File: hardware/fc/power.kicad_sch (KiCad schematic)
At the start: 26 parts, among them U1 TPS7A8101DRBR, U2 TPS7A8101DRBR, U3 LMR51420YFDDCR

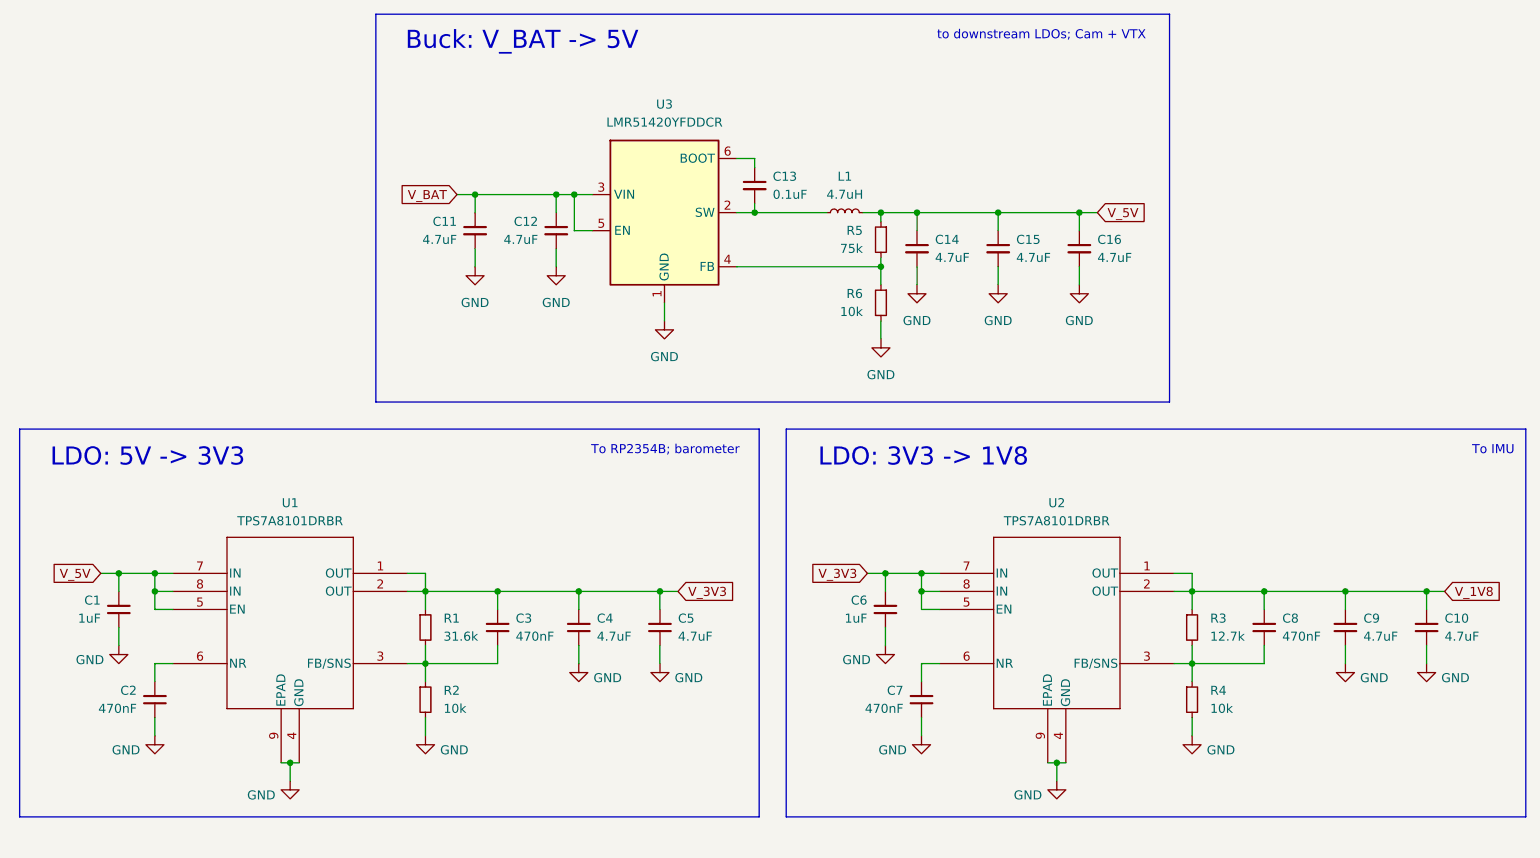
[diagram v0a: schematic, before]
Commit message: fc: add peripherals and sensors
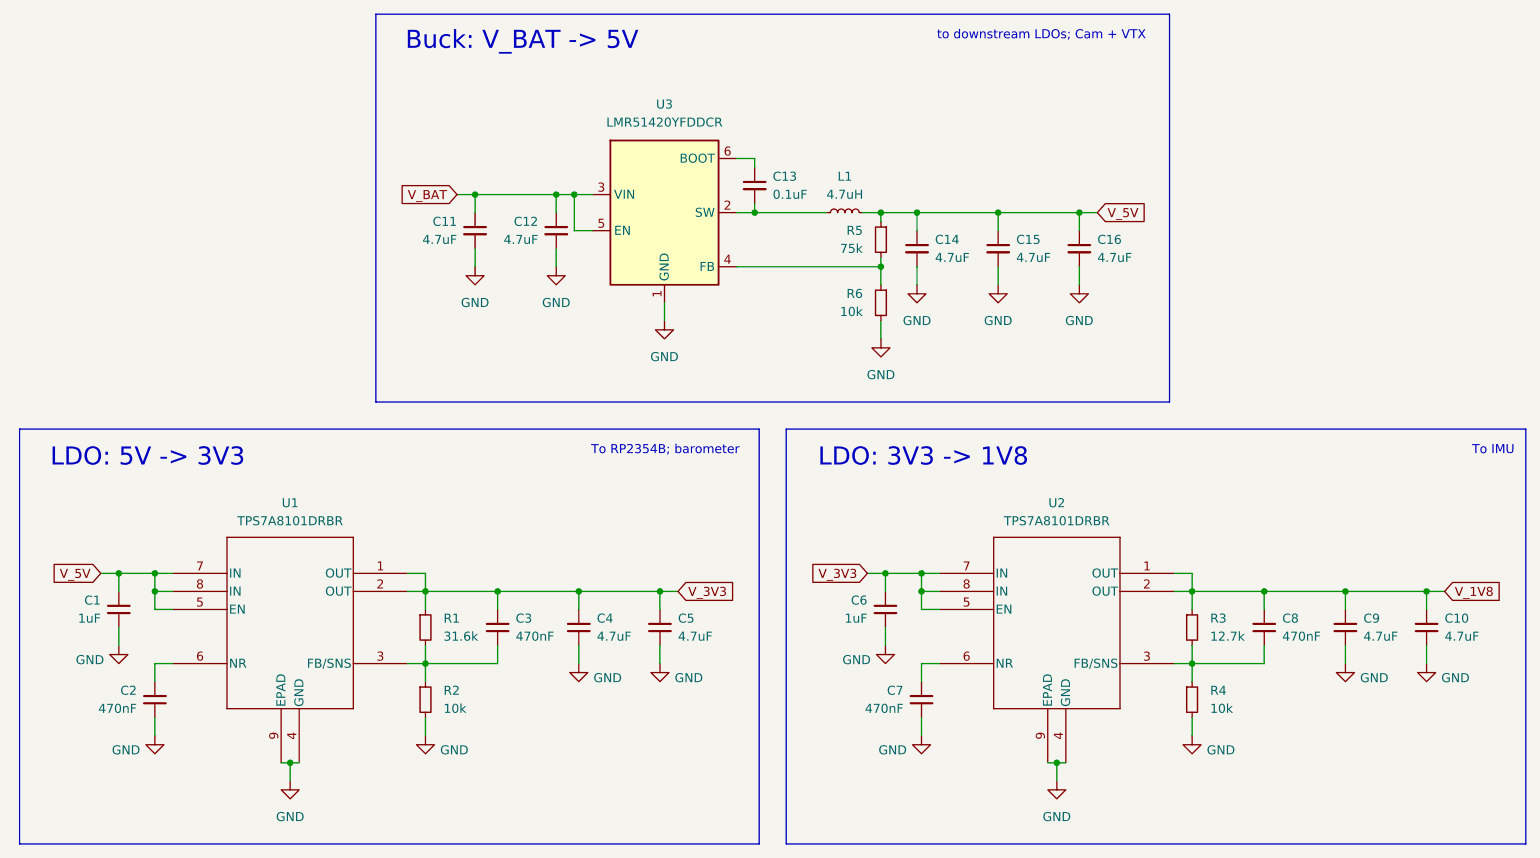
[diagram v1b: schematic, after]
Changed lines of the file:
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@@
 	(rectangle
 		(start 149.86 92.71)
-		(end 254 147.32)
+		(end 254 151.13)
 		(stroke
 			(width 0)
@@
 	(rectangle
 		(start 41.91 92.71)
-		(end 146.05 147.32)
+		(end 146.05 151.13)
 		(stroke
 			(width 0)
@@
 	(symbol
 		(lib_id "power:GND")
-		(at 187.96 142.24 0)
-		(unit 1)
-		(body_style 1)
-		(exclude_from_sim no)
-		(in_bom yes)
-		(on_board yes)
-		(in_pos_files yes)
-		(dnp no)
-		(property "Reference" "#PWR08"
-			(at 187.96 148.59 0)
-			(hide yes)
-			(show_name no)
-			(do_not_autoplace no)
-			(effects
-				(font
-					(size 1.27 1.27)
-				)
-			)
-		)
-		(property "Value" "GND"
-			(at 183.896 144.272 0)
-			(show_name no)
-			(do_not_autoplace no)
-			(effects
-				(font
-					(size 1.27 1.27)
-				)
-			)
-		)
-		(property "Footprint" ""
-			(at 187.96 142.24 0)
-			(hide yes)
-			(show_name no)
-			(do_not_autoplace no)
-			(effects
-				(font
-					(size 1.27 1.27)
-				)
-			)
-		)
-		(property "Datasheet" ""
-			(at 187.96 142.24 0)
-			(hide yes)
-			(show_name no)
-			(do_not_autoplace no)
-			(effects
-				(font
-					(size 1.27 1.27)
-				)
-			)
-		)
-		(property "Description" "Power symbol creates a global label with name \"GND\" , ground"
-			(at 187.96 142.24 0)
-			(hide yes)
-			(show_name no)
-			(do_not_autoplace no)
-			(effects
-				(font
-					(size 1.27 1.27)
-				)
-			)
-		)
-		(pin "1"
-		)
-		(instances
-			(project "fc"
-				(path "/6eb6d89e-9d71-4347-9ba3-a394c00e5720/e2294782-fc96-4933-bb6d-aced2c760448"
-					(reference "#PWR08")
-					(unit 1)
-				)
-			)
-		)
-	)
-	(symbol
-		(lib_id "power:GND")
 		(at 120.65 125.73 0)
 		(mirror y)
@@
 	(symbol
 		(lib_id "power:GND")
-		(at 132.715 77.47 0)
+		(at 187.96 142.24 0)
 		(unit 1)
 		(body_style 1)
@@
 		(dnp no)
 		(fields_autoplaced yes)
-		(property "Reference" "#PWR065"
-			(at 132.715 83.82 0)
+		(property "Reference" "#PWR08"
+			(at 187.96 148.59 0)
 			(hide yes)
 			(show_name no)
@@
 		)
 		(property "Value" "GND"
-			(at 132.715 82.55 0)
+			(at 187.96 147.32 0)
 			(show_name no)
 			(do_not_autoplace no)
@@
 		)
 		(property "Footprint" ""
-			(at 132.715 77.47 0)
+			(at 187.96 142.24 0)
 			(hide yes)
 			(show_name no)
@@
 		)
 		(property "Datasheet" ""
-			(at 132.715 77.47 0)
+			(at 187.96 142.24 0)
 			(hide yes)
 			(show_name no)
@@
 		)
 		(property "Description" "Power symbol creates a global label with name \"GND\" , ground"
-			(at 132.715 77.47 0)
+			(at 187.96 142.24 0)
 			(hide yes)
 			(show_name no)
@@
 			(project "fc"
 				(path "/6eb6d89e-9d71-4347-9ba3-a394c00e5720/e2294782-fc96-4933-bb6d-aced2c760448"
-					(reference "#PWR065")
+					(reference "#PWR08")
 					(unit 1)
 				)
@@
 	)
 	(symbol
-		(lib_name "C_Small_6")
-		(lib_id "Device:C_Small")
-		(at 117.475 64.77 0)
-		(mirror y)
+		(lib_id "power:GND")
+		(at 132.715 77.47 0)
 		(unit 1)
 		(body_style 1)
@@
 		(in_pos_files yes)
 		(dnp no)
-		(property "Reference" "C12"
-			(at 114.935 63.5062 0)
+		(fields_autoplaced yes)
+		(property "Reference" "#PWR065"
+			(at 132.715 83.82 0)
+			(hide yes)
 			(show_name no)
 			(do_not_autoplace no)
@@
 					(size 1.27 1.27)
 				)
-				(justify left)
 			)
 		)
-		(property "Value" "4.7uF"
-			(at 114.935 66.0462 0)
+		(property "Value" "GND"
+			(at 132.715 82.55 0)
 			(show_name no)
 			(do_not_autoplace no)
@@
 					(size 1.27 1.27)
 				)
-				(justify left)
 			)
 		)
-		(property "Footprint" "Capacitor_SMD:C_0603_1608Metric"
-			(at 117.475 64.77 0)
+		(property "Footprint" ""
+			(at 132.715 77.47 0)
 			(hide yes)
 			(show_name no)
@@
 		)
 		(property "Datasheet" ""
-			(at 117.475 64.77 0)
+			(at 132.715 77.47 0)
 			(hide yes)
 			(show_name no)
@@
 			)
 		)
-		(property "Description" "0603 4.7uF 35V"
-			(at 117.475 64.77 0)
+		(property "Description" "Power symbol creates a global label with name \"GND\" , ground"
+			(at 132.715 77.47 0)
 			(hide yes)
 			(show_name no)
@@
 			)
 		)
-		(property "LCSC#" "C307467"
-			(at 117.475 64.77 0)
+		(pin "1"
+		)
+		(instances
+			(project "fc"
+				(path "/6eb6d89e-9d71-4347-9ba3-a394c00e5720/e2294782-fc96-4933-bb6d-aced2c760448"
+					(reference "#PWR065")
+					(unit 1)
+				)
+			)
+		)
+	)
+	(symbol
+		(lib_id "power:GND")
+		(at 80.01 142.24 0)
+		(unit 1)
+		(body_style 1)
+		(exclude_from_sim no)
+		(in_bom yes)
+		(on_board yes)
+		(in_pos_files yes)
+		(dnp no)
+		(fields_autoplaced yes)
+		(property "Reference" "#PWR03"
+			(at 80.01 148.59 0)
 			(hide yes)
 			(show_name no)
@@
 			)
 		)
-		(property "MFR" "Samsung"
-			(at 117.475 64.77 0)
+		(property "Value" "GND"
+			(at 80.01 147.32 0)
+			(show_name no)
+			(do_not_autoplace no)
+			(effects
+				(font
+					(size 1.27 1.27)
+				)
+			)
+		)
+		(property "Footprint" ""
+			(at 80.01 142.24 0)
 			(hide yes)
 			(show_name no)
@@
 			)
 		)
-		(property "MPN" "CL10A475KL8NRNC"
-			(at 117.475 64.77 0)
+		(property "Datasheet" ""
+			(at 80.01 142.24 0)
 			(hide yes)
 			(show_name no)
@@
 			)
 		)
-		(pin "1"
+		(property "Description" "Power symbol creates a global label with name \"GND\" , ground"
+			(at 80.01 142.24 0)
+			(hide yes)
+			(show_name no)
+			(do_not_autoplace no)
+			(effects
+				(font
+					(size 1.27 1.27)
+				)
+			)
 		)
-		(pin "2"
+		(pin "1"
 		)
 		(instances
 			(project "fc"
 				(path "/6eb6d89e-9d71-4347-9ba3-a394c00e5720/e2294782-fc96-4933-bb6d-aced2c760448"
-					(reference "C12")
+					(reference "#PWR03")
 					(unit 1)
 				)
@@
 	)
 	(symbol
-		(lib_id "Device:R_Small")
-		(at 99.06 120.65 0)
+		(lib_name "C_Small_6")
+		(lib_id "Device:C_Small")
+		(at 117.475 64.77 0)
+		(mirror y)
 		(unit 1)
 		(body_style 1)
@@
 		(in_pos_files yes)
 		(dnp no)
-		(fields_autoplaced yes)
-		(property "Reference" "R1"
-			(at 101.6 119.3799 0)
+		(property "Reference" "C12"
+			(at 114.935 63.5062 0)
 			(show_name no)
 			(do_not_autoplace no)
@@
 			)
 		)
-		(property "Value" "31.6k"
-			(at 101.6 121.9199 0)
+		(property "Value" "4.7uF"
+			(at 114.935 66.0462 0)
 			(show_name no)
 			(do_not_autoplace no)
@@
 			)
 		)
-		(property "Footprint" ""
-			(at 99.06 120.65 0)
+		(property "Footprint" "Capacitor_SMD:C_0603_1608Metric"
+			(at 117.475 64.77 0)
 			(hide yes)
 			(show_name no)
@@
 		)
 		(property "Datasheet" ""
-			(at 99.06 120.65 0)
+			(at 117.475 64.77 0)
 			(hide yes)
 			(show_name no)
@@
 			)
 		)
-		(property "Description" "Resistor, small symbol"
-			(at 99.06 120.65 0)
+		(property "Description" "0603 4.7uF 35V"
+			(at 117.475 64.77 0)
+			(hide yes)
+			(show_name no)
+			(do_not_autoplace no)
+			(effects
+				(font
+					(size 1.27 1.27)
+				)
+			)
+		)
+		(property "LCSC#" "C307467"
+			(at 117.475 64.77 0)
+			(hide yes)
+			(show_name no)
+			(do_not_autoplace no)
+			(effects
+				(font
+					(size 1.27 1.27)
+				)
+			)
+		)
+		(property "MFR" "Samsung"
+			(at 117.475 64.77 0)
+			(hide yes)
+			(show_name no)
+			(do_not_autoplace no)
+			(effects
+				(font
+					(size 1.27 1.27)
+				)
+			)
+		)
+		(property "MPN" "CL10A475KL8NRNC"
+			(at 117.475 64.77 0)
 			(hide yes)
 			(show_name no)
@@
 			(project "fc"
 				(path "/6eb6d89e-9d71-4347-9ba3-a394c00e5720/e2294782-fc96-4933-bb6d-aced2c760448"
-					(reference "R1")
+					(reference "C12")
 					(unit 1)
 				)
@@
 	)
 	(symbol
-		(lib_id "power:GND")
-		(at 80.01 142.24 0)
+		(lib_id "Device:R_Small")
+		(at 99.06 120.65 0)
 		(unit 1)
 		(body_style 1)
@@
 		(in_pos_files yes)
 		(dnp no)
-		(property "Reference" "#PWR03"
-			(at 80.01 148.59 0)
-			(hide yes)
+		(fields_autoplaced yes)
+		(property "Reference" "R1"
+			(at 101.6 119.3799 0)
 			(show_name no)
 			(do_not_autoplace no)
@@
 					(size 1.27 1.27)
 				)
+				(justify left)
 			)
 		)
-		(property "Value" "GND"
-			(at 75.946 144.272 0)
+		(property "Value" "31.6k"
+			(at 101.6 121.9199 0)
 			(show_name no)
 			(do_not_autoplace no)
@@
 					(size 1.27 1.27)
 				)
+				(justify left)
 			)
 		)
 		(property "Footprint" ""
-			(at 80.01 142.24 0)
+			(at 99.06 120.65 0)
 			(hide yes)
 			(show_name no)
@@
 		)
 		(property "Datasheet" ""
-			(at 80.01 142.24 0)
+			(at 99.06 120.65 0)
 			(hide yes)
 			(show_name no)
@@
 			)
 		)
-		(property "Description" "Power symbol creates a global label with name \"GND\" , ground"
-			(at 80.01 142.24 0)
+		(property "Description" "Resistor, small symbol"
+			(at 99.06 120.65 0)
 			(hide yes)
 			(show_name no)
@@
 		(pin "1"
 		)
+		(pin "2"
+		)
 		(instances
 			(project "fc"
 				(path "/6eb6d89e-9d71-4347-9ba3-a394c00e5720/e2294782-fc96-4933-bb6d-aced2c760448"
-					(reference "#PWR03")
+					(reference "R1")
 					(unit 1)
 				)

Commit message: fc: add 5V mux and OSD
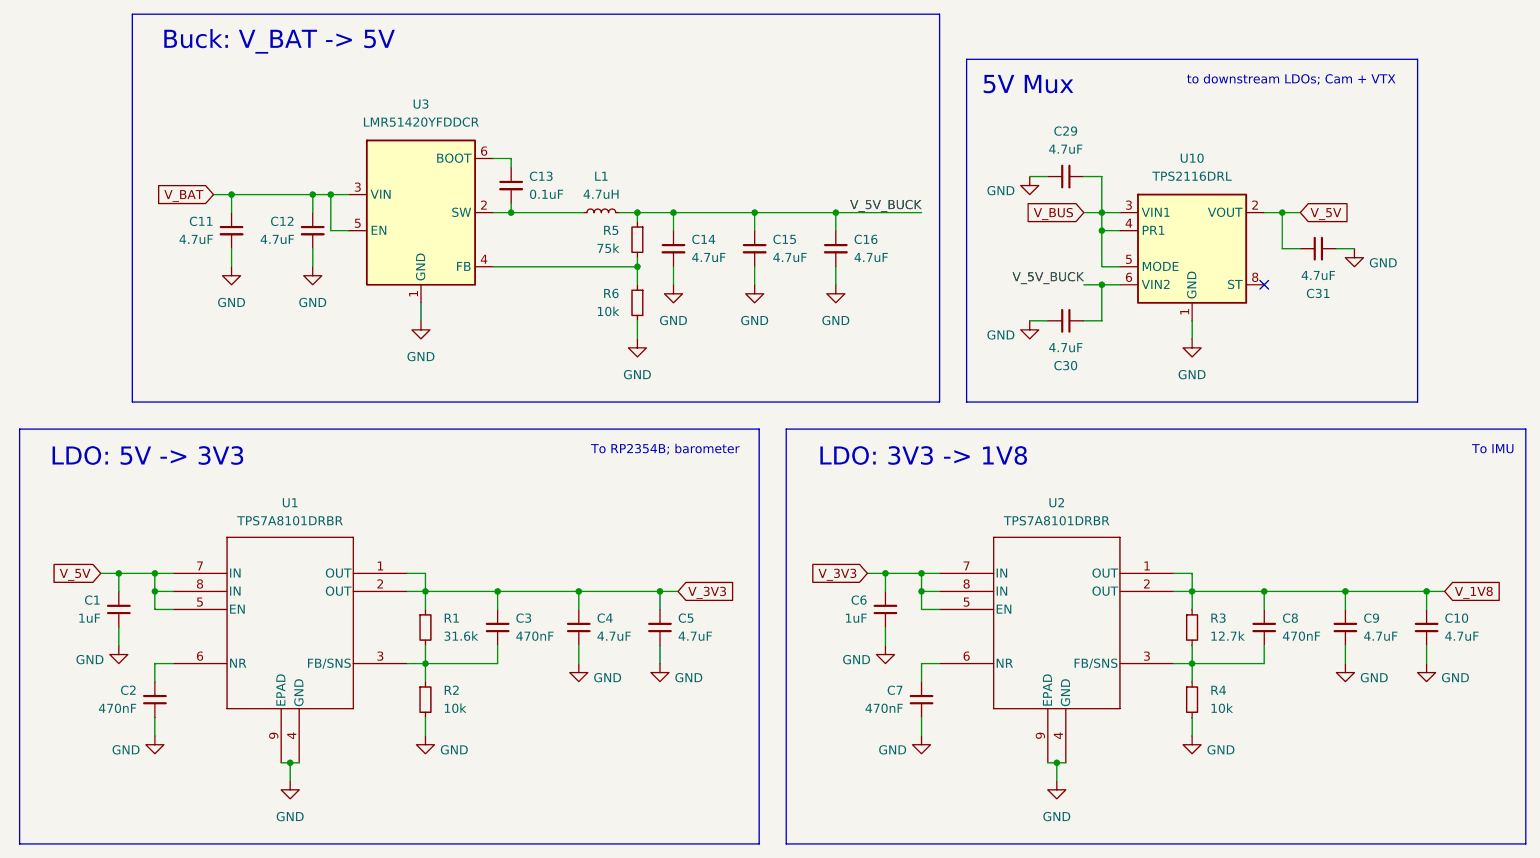
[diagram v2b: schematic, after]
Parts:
- added C29, C30, C31: 4.7uF, Package_TO_SOT_SMD:SOT-583-8, symbol Device:C_Small
- added U10: TPS2116DRL, Package_TO_SOT_SMD:SOT-583-8, symbol Power_Management:TPS2116DRL
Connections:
- net GND: now also C29.2, C30.2, C31.2, U10.1 (GND)
- net V_5V: now also C31.1, U10.2 (VOUT), U10.7 (VOUT); no longer C14.1, C15.1, C16.1, L1.2, R5.1
- new net V_5V_BUCK: C14.1, C15.1, C16.1, C30.1, L1.2, R5.1, U10.6 (VIN2)
- new net V_BUS: C29.1, U10.3 (VIN1), U10.4 (PR1), U10.5 (MODE)
- no-connect marks 0 -> 1
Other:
- note added: "5V Mux"
- moved on the sheet: C11, C12, C13, C14, C15, C16, L1, R5, R6, U3

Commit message: fc: delete barometer; finalise schematic
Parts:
- R3: value 12.7k -> 31.6k
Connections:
- net V_3V3: no longer C6.1, U2.5 (EN), U2.7 (IN), U2.8 (IN)
- net V_5V: now also C6.1, U2.5 (EN), U2.7 (IN), U2.8 (IN)
- net V_1V8 renamed V_IMU
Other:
- note added: "To RP2354B"
- note removed: "LDO: 3V3 -> 1V8"
- note removed: "To RP2354B; barometer"
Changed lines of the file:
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@@
 		)
 	)
-	(text "To RP2354B; barometer"
+	(text "To RP2354B\n"
 		(exclude_from_sim no)
-		(at 132.842 95.758 0)
+		(at 138.43 95.758 0)
 		(effects
 			(font
@@
 		)
 	)
-	(text "LDO: 3V3 -> 1V8"
+	(text "LDO: 5V -> 3V3"
 		(exclude_from_sim no)
-		(at 169.164 96.774 0)
+		(at 167.894 96.774 0)
 		(effects
 			(font
@@
 		)
 	)
-	(global_label "V_3V3"
+	(global_label "V_BUS"
 		(shape input)
-		(at 161.29 113.03 180)
+		(at 191.77 62.23 180)
 		(fields_autoplaced yes)
 		(effects
@@
 		)
 		(property "Intersheetrefs" "${INTERSHEET_REFS}"
-			(at 152.741 113.03 0)
+			(at 182.9186 62.23 0)
 			(hide yes)
 			(show_name no)
@@
 		)
 	)
-	(global_label "V_BUS"
+	(global_label "V_3V3"
 		(shape input)
-		(at 191.77 62.23 180)
+		(at 134.62 115.57 0)
 		(fields_autoplaced yes)
 		(effects
@@
 				(size 1.27 1.27)
 			)
-			(justify right)
+			(justify left)
 		)
 		(property "Intersheetrefs" "${INTERSHEET_REFS}"
-			(at 182.9186 62.23 0)
+			(at 143.169 115.57 0)
 			(hide yes)
 			(show_name no)
@@
 					(size 1.27 1.27)
 				)
-				(justify right)
+				(justify left)
 			)
 		)
 	)
-	(global_label "V_3V3"
+	(global_label "V_5V"
 		(shape input)
-		(at 134.62 115.57 0)
+		(at 53.34 113.03 180)
 		(fields_autoplaced yes)
 		(effects
@@
 				(size 1.27 1.27)
 			)
-			(justify left)
+			(justify right)
 		)
 		(property "Intersheetrefs" "${INTERSHEET_REFS}"
-			(at 143.169 115.57 0)
+			(at 46.0005 113.03 0)
 			(hide yes)
 			(show_name no)
@@
 					(size 1.27 1.27)
 				)
-				(justify left)
+				(justify right)
 			)
 		)
@@
 	(global_label "V_5V"
 		(shape input)
-		(at 53.34 113.03 180)
+		(at 161.29 113.03 180)
 		(fields_autoplaced yes)
 		(effects
@@
 		)
 		(property "Intersheetrefs" "${INTERSHEET_REFS}"
-			(at 46.0005 113.03 0)
+			(at 153.9505 113.03 0)
 			(hide yes)
 			(show_name no)
@@
 		)
 	)
-	(global_label "V_1V8"
+	(global_label "V_IMU"
 		(shape input)
 		(at 242.57 115.57 0)
@@
 		)
 		(property "Intersheetrefs" "${INTERSHEET_REFS}"
-			(at 251.119 115.57 0)
+			(at 250.9981 115.57 0)
 			(hide yes)
 			(show_name no)
@@
 			)
 		)
-		(property "Value" "12.7k"
+		(property "Value" "31.6k"
 			(at 209.55 121.9199 0)
 			(show_name no)

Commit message: fc: add footprints
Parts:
- C1, C10, C2, C3, C4, C5, C6, C7, C8, C9: footprint (none) -> Stratus:C_0402
- C29, C30, C31: footprint Package_TO_SOT_SMD:SOT-583-8 -> Stratus:C_0402
- R1, R2, R3, R4: footprint (none) -> Stratus:R_0402
- U1, U2: footprint Stratus:LDLPUR212 -> Package_SON:VSON-8-1EP_3x3mm_P0.65mm_EP1.65x2.4mm
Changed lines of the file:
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@@
 			)
 		)
-		(property "Footprint" ""
+		(property "Footprint" "Stratus:C_0402"
 			(at 240.03 120.65 0)
 			(hide yes)
@@
 			)
 		)
-		(property "Footprint" ""
+		(property "Footprint" "Stratus:C_0402"
 			(at 60.96 130.81 0)
 			(hide yes)
@@
 			)
 		)
-		(property "Footprint" ""
+		(property "Footprint" "Stratus:C_0402"
 			(at 163.83 118.11 0)
 			(hide yes)
@@
 			)
 		)
-		(property "Footprint" ""
+		(property "Footprint" "Stratus:C_0402"
 			(at 217.17 120.65 0)
 			(hide yes)
@@
 			)
 		)
-		(property "Footprint" ""
+		(property "Footprint" "Stratus:C_0402"
 			(at 120.65 120.65 0)
 			(hide yes)
@@
 			)
 		)
-		(property "Footprint" ""
+		(property "Footprint" "Stratus:R_0402"
 			(at 99.06 130.81 0)
 			(hide yes)
@@
 			)
 		)
-		(property "Footprint" "Package_TO_SOT_SMD:SOT-583-8"
+		(property "Footprint" "Stratus:C_0402"
 			(at 224.79 67.31 0)
 			(hide yes)
@@
 			)
 		)
-		(property "Footprint" ""
+		(property "Footprint" "Stratus:C_0402"
 			(at 109.22 120.65 0)
 			(hide yes)
@@
 			)
 		)
-		(property "Footprint" ""
+		(property "Footprint" "Stratus:R_0402"
 			(at 99.06 120.65 0)
 			(hide yes)
@@
 			)
 		)
-		(property "Footprint" "Stratus:LDLPUR212"
+		(property "Footprint" "Package_SON:VSON-8-1EP_3x3mm_P0.65mm_EP1.65x2.4mm"
 			(at 130.81 114.3 0)
 			(hide yes)
@@
 			)
 		)
-		(property "Footprint" ""
+		(property "Footprint" "Stratus:C_0402"
 			(at 228.6 120.65 0)
 			(hide yes)
@@
 			)
 		)
-		(property "Footprint" ""
+		(property "Footprint" "Stratus:R_0402"
 			(at 207.01 130.81 0)
 			(hide yes)
@@
 			)
 		)
-		(property "Footprint" "Package_TO_SOT_SMD:SOT-583-8"
+		(property "Footprint" "Stratus:C_0402"
 			(at 189.23 57.15 0)
 			(hide yes)
@@
 			)
 		)
-		(property "Footprint" ""
+		(property "Footprint" "Stratus:C_0402"
 			(at 55.88 118.11 0)
 			(hide yes)
@@
 			)
 		)
-		(property "Footprint" ""
+		(property "Footprint" "Stratus:C_0402"
 			(at 132.08 120.65 0)
 			(hide yes)
@@
 			)
 		)
-		(property "Footprint" "Package_TO_SOT_SMD:SOT-583-8"
+		(property "Footprint" "Stratus:C_0402"
 			(at 189.23 77.47 0)
 			(hide yes)
@@
 			)
 		)
-		(property "Footprint" ""
+		(property "Footprint" "Stratus:C_0402"
 			(at 168.91 130.81 0)
 			(hide yes)
@@
 			)
 		)
-		(property "Footprint" ""
+		(property "Footprint" "Stratus:R_0402"
 			(at 207.01 120.65 0)
 			(hide yes)
@@
 			)
 		)
-		(property "Footprint" "Stratus:LDLPUR212"
+		(property "Footprint" "Package_SON:VSON-8-1EP_3x3mm_P0.65mm_EP1.65x2.4mm"
 			(at 238.76 114.3 0)
 			(hide yes)
